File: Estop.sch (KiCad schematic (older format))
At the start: 0 parts

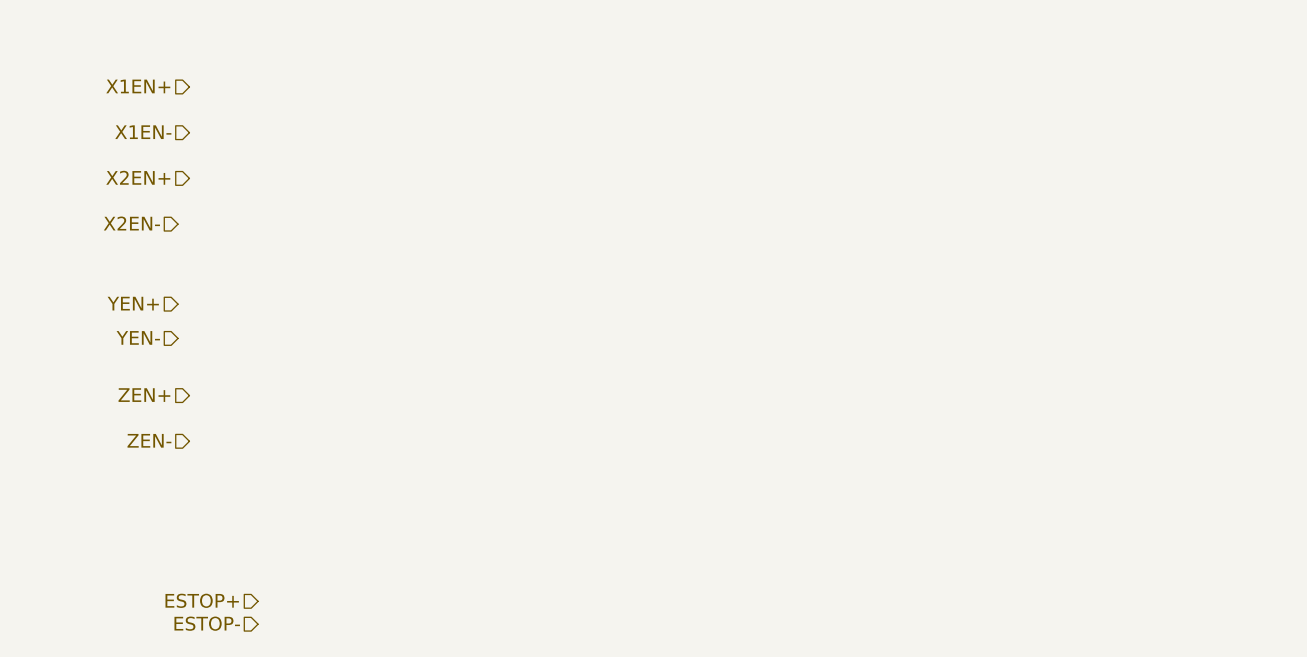
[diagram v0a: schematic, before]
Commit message: added opto and DE footprints
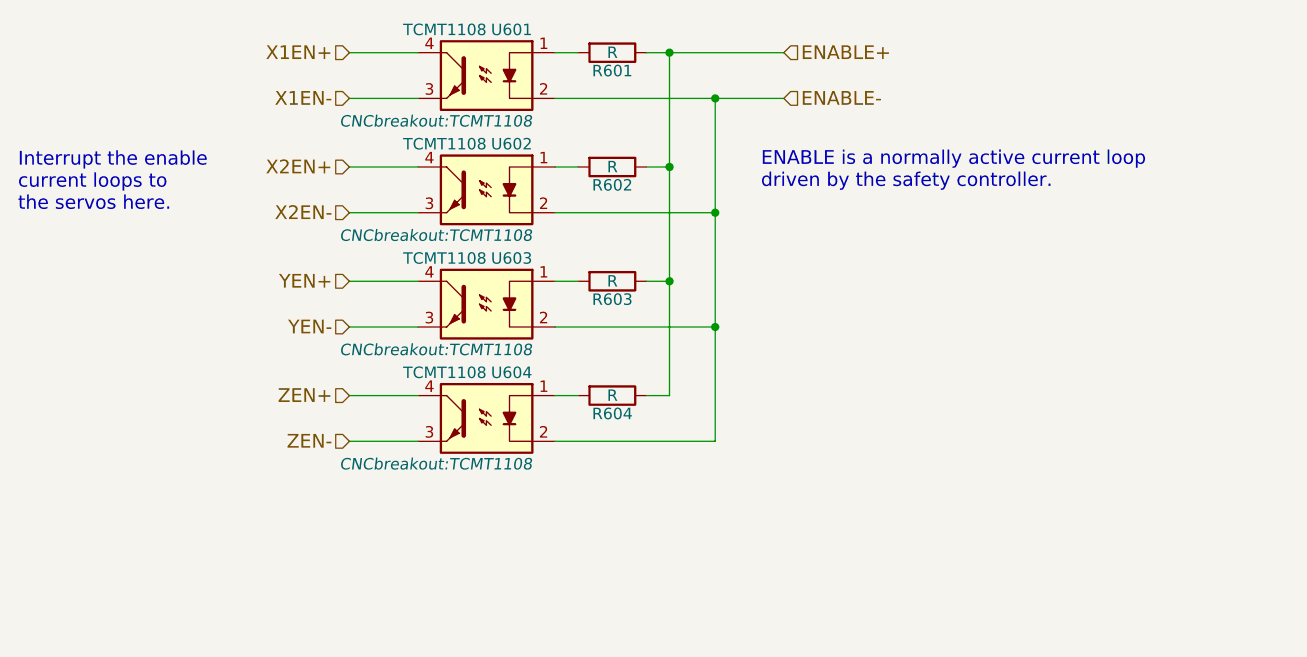
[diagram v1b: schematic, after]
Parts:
- added R601, R602, R603, R604: R, Resistors_SMD:R_1206, symbol R
- added U601, U602, U603, U604: TCMT1108, CNCbreakout:TCMT1108, symbol TLP291
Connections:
- net X1EN+: now also U601.4
- net X1EN-: now also U601.3
- net X2EN+: now also U602.4
- net X2EN-: now also U602.3
- net YEN+: now also U603.4
- net YEN-: now also U603.3
- net ZEN+: now also U604.4
- net ZEN-: now also U604.3
- new net: R601.2, U601.1
- new net: R602.2, U602.1
- new net: R603.2, U603.1
- new net: R604.2, U604.1
- new net ENABLE+: R601.1, R602.1, R603.1, R604.1
- new net ENABLE-: U601.2, U602.2, U603.2, U604.2
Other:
- note added: "ENABLE is a normally active current loop\ndriven by the safety controller."
- note added: "Interrupt the enable\ncurrent loops to\nthe servos here."
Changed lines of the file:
@@
 LIBS:valves
 LIBS:references
+LIBS:FabLab
 LIBS:CNCbreakout-cache
 EELAYER 25 0
@@
 Comment4 ""
 $EndDescr
-Text HLabel 1800 3000 0    60   Input ~ 0
+Text HLabel 2500 3000 0    60   Input ~ 0
 ZEN+
-Text HLabel 1800 3200 0    60   Input ~ 0
+Text HLabel 2500 3200 0    60   Input ~ 0
 ZEN-
-Text HLabel 1750 2600 0    60   Input ~ 0
+Text HLabel 2500 2500 0    60   Input ~ 0
 YEN+
-Text HLabel 1750 2750 0    60   Input ~ 0
+Text HLabel 2500 2700 0    60   Input ~ 0
 YEN-
-Text HLabel 1800 1650 0    60   Input ~ 0
+Text HLabel 2500 1500 0    60   Input ~ 0
 X1EN+
-Text HLabel 1800 1850 0    60   Input ~ 0
+Text HLabel 2500 1700 0    60   Input ~ 0
 X1EN-
-Text HLabel 1800 2050 0    60   Input ~ 0
+Text HLabel 2500 2000 0    60   Input ~ 0
 X2EN+
-Text HLabel 1750 2250 0    60   Input ~ 0
+Text HLabel 2500 2200 0    60   Input ~ 0
 X2EN-
-Text HLabel 2100 3900 0    60   Input ~ 0
-ESTOP+
-Text HLabel 2100 4000 0    60   Input ~ 0
-ESTOP-
+Text HLabel 4400 1500 2    60   Input ~ 0
+ENABLE+
+Text HLabel 4400 1700 2    60   Input ~ 0
+ENABLE-
+$Comp
+L R R601
+U 1 1 57B7DBC7
+P 3650 1500
+F 0 "R601" V 3730 1500 50  0000 C CNN
+F 1 "R" V 3650 1500 50  0000 C CNN
+F 2 "Resistors_SMD:R_1206" V 3580 1500 50  0001 C CNN
+F 3 "" H 3650 1500 50  0000 C CNN
+	1    3650 1500
+	0    1    1    0
+$EndComp
+$Comp
+L R R602
+U 1 1 57B7DC17
+P 3650 2000
+F 0 "R602" V 3730 2000 50  0000 C CNN
+F 1 "R" V 3650 2000 50  0000 C CNN
+F 2 "Resistors_SMD:R_1206" V 3580 2000 50  0001 C CNN
+F 3 "" H 3650 2000 50  0000 C CNN
+	1    3650 2000
+	0    1    1    0
+$EndComp
+$Comp
+L R R603
+U 1 1 57B7DC49
+P 3650 2500
+F 0 "R603" V 3730 2500 50  0000 C CNN
+F 1 "R" V 3650 2500 50  0000 C CNN
+F 2 "Resistors_SMD:R_1206" V 3580 2500 50  0001 C CNN
+F 3 "" H 3650 2500 50  0000 C CNN
+	1    3650 2500
+	0    1    1    0
+$EndComp
+$Comp
+L R R604
+U 1 1 57B7DC7E
+P 3650 3000
+F 0 "R604" V 3730 3000 50  0000 C CNN
+F 1 "R" V 3650 3000 50  0000 C CNN
+F 2 "Resistors_SMD:R_1206" V 3580 3000 50  0001 C CNN
+F 3 "" H 3650 3000 50  0000 C CNN
+	1    3650 3000
+	0    1    1    0
+$EndComp
+Wire Wire Line
+	3800 1500 4400 1500
+Wire Wire Line
+	3500 1500 3400 1500
+Wire Wire Line
+	3400 1700 4400 1700
+Wire Wire Line
+	3900 1500 3900 3000
+Wire Wire Line
+	3900 3000 3800 3000
+Connection ~ 3900 1500
+Wire Wire Line
+	3800 2500 3900 2500
+Connection ~ 3900 2500
+Wire Wire Line
+	3900 2000 3800 2000
+Connection ~ 3900 2000
+Wire Wire Line
+	3500 2000 3400 2000
+Wire Wire Line
+	3400 2500 3500 2500
+Wire Wire Line
+	3500 3000 3400 3000
+Wire Wire Line
+	4100 3200 3400 3200
+Wire Wire Line
+	4100 1700 4100 3200
+Connection ~ 4100 1700
+Wire Wire Line
+	4100 2200 3400 2200
+Connection ~ 4100 2200
+Wire Wire Line
+	3400 2700 4100 2700
+Connection ~ 4100 2700
+Wire Wire Line
+	2500 1500 2800 1500
+Wire Wire Line
+	2800 1700 2500 1700
+Wire Wire Line
+	2500 2000 2800 2000
+Wire Wire Line
+	2800 2200 2500 2200
+Wire Wire Line
+	2500 2500 2800 2500
+Wire Wire Line
+	2800 2700 2500 2700
+Wire Wire Line
+	2500 3000 2800 3000
+Wire Wire Line
+	2800 3200 2500 3200
+Text Notes 4300 2100 0    60   ~ 0
+ENABLE is a normally active current loop\ndriven by the safety controller.
+Text Notes 1050 2200 0    60   ~ 0
+Interrupt the enable\ncurrent loops to\nthe servos here.
+$Comp
+L TLP291 U601
+U 1 1 57BB01CB
+P 3100 1600
+F 0 "U601" H 2900 1800 50  0000 L CNN
+F 1 "TCMT1108" H 3100 1800 50  0000 L CNN
+F 2 "CNCbreakout:TCMT1108" H 2900 1400 50  0000 L CIN
+F 3 "" H 3100 1600 50  0000 L CNN
+	1    3100 1600
+	-1   0    0    -1
+$EndComp
+$Comp
+L TLP291 U602
+U 1 1 57BB0327
+P 3100 2100
+F 0 "U602" H 2900 2300 50  0000 L CNN
+F 1 "TCMT1108" H 3100 2300 50  0000 L CNN
+F 2 "CNCbreakout:TCMT1108" H 2900 1900 50  0000 L CIN
+F 3 "" H 3100 2100 50  0000 L CNN
+	1    3100 2100
+	-1   0    0    -1
+$EndComp
+$Comp
+L TLP291 U603
+U 1 1 57BB03C8
+P 3100 2600
+F 0 "U603" H 2900 2800 50  0000 L CNN
+F 1 "TCMT1108" H 3100 2800 50  0000 L CNN
+F 2 "CNCbreakout:TCMT1108" H 2900 2400 50  0000 L CIN
+F 3 "" H 3100 2600 50  0000 L CNN
+	1    3100 2600
+	-1   0    0    -1
+$EndComp
+$Comp
+L TLP291 U604
+U 1 1 57BB04A9
+P 3100 3100
+F 0 "U604" H 2900 3300 50  0000 L CNN
+F 1 "TCMT1108" H 3100 3300 50  0000 L CNN
+F 2 "CNCbreakout:TCMT1108" H 2900 2900 50  0000 L CIN
+F 3 "" H 3100 3100 50  0000 L CNN
+	1    3100 3100
+	-1   0    0    -1
+$EndComp
 $EndSCHEMATC
